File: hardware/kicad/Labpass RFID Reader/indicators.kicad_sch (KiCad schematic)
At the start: 8 parts

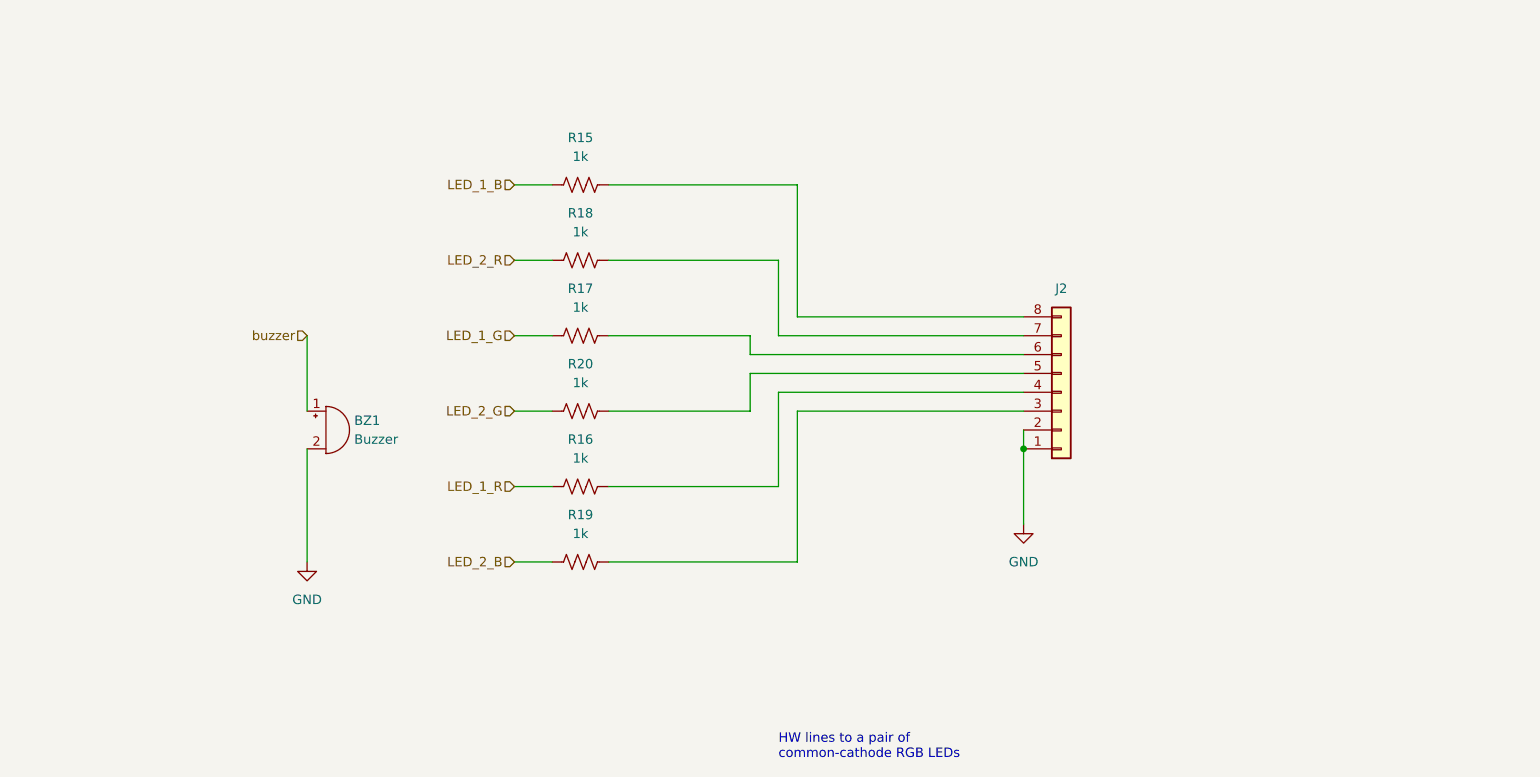
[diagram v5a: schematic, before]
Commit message: Add terminal block for gpio to ext relay
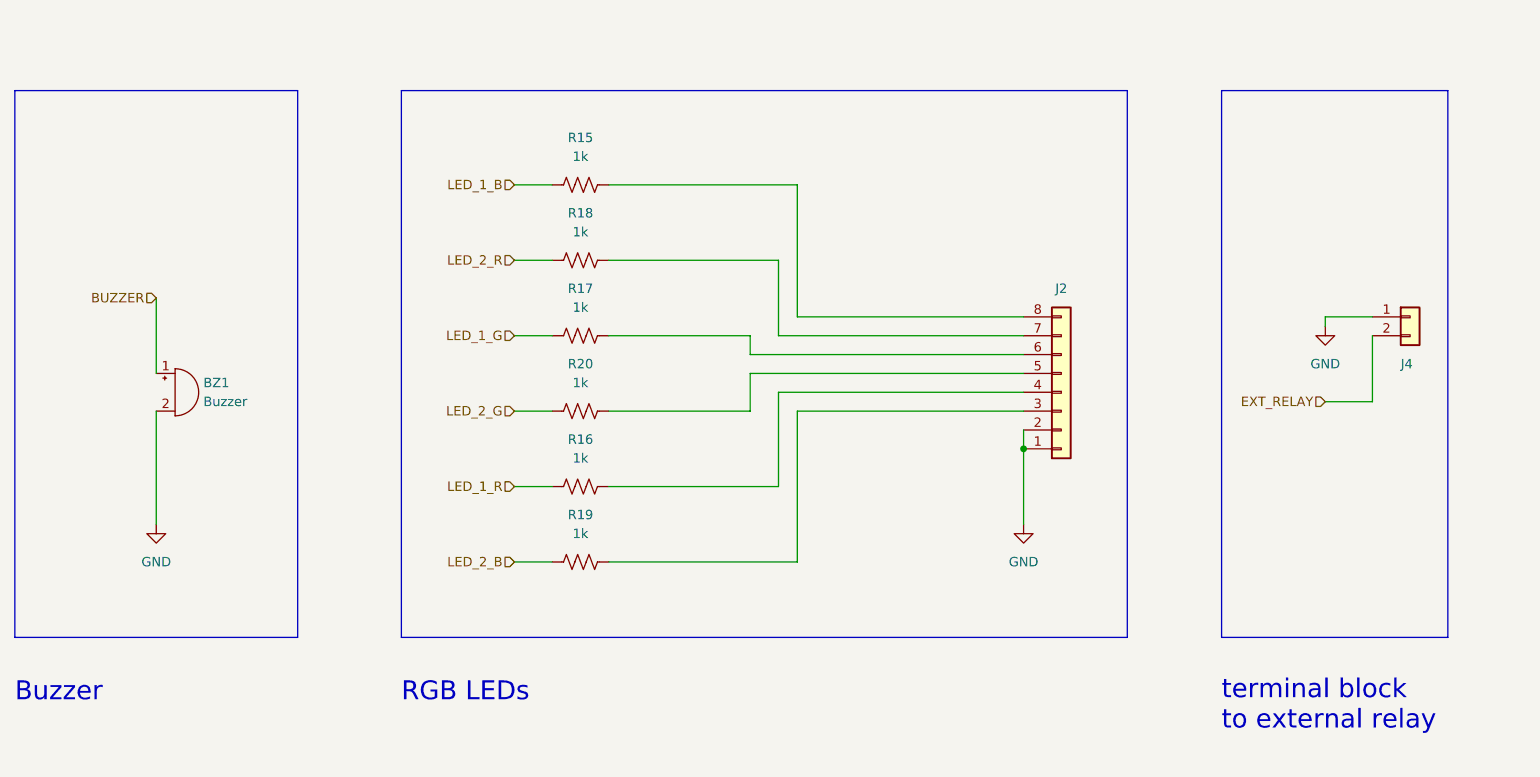
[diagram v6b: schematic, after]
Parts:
- added J4: (no value), symbol Connector_Generic:Conn_01x02
- J2: value (none) -> Conn_01x08; footprint (none) -> Connector_PinHeader_2.54mm:PinHeader_2x04_P2.54mm_Horizontal
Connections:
- net GND: now also J4.1 (Pin_1)
- net buzzer renamed BUZZER
- new net EXT_RELAY: J4.2 (Pin_2)
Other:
- note added: "Buzzer"
- note added: "RGB LEDs"
- note added: "terminal block to external relay"
- note removed: "HW lines to a pair of common-cathode RGB LEDs"
- moved on the sheet: BZ1
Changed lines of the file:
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@@
   (junction (at 167.64 97.79) (diameter 0) (color 0 0 0 0)
   )
+  (polyline (pts (xy 83.82 123.19) (xy 181.61 123.19))
+    (stroke (width 0) (type default) (color 0 0 0 0))
+  )
   (wire (pts (xy 130.81 92.71) (xy 130.81 87.63))
     (stroke (width 0) (type default) (color 0 0 0 0))
   )
-  (wire (pts (xy 71.12 82.55) (xy 71.12 92.71))
+  (wire (pts (xy 50.8 77.47) (xy 50.8 87.63))
+    (stroke (width 0) (type default) (color 0 0 0 0))
+  )
+  (polyline (pts (xy 31.75 49.53) (xy 31.75 123.19))
     (stroke (width 0) (type default) (color 0 0 0 0))
   )
@@
     (stroke (width 0) (type default) (color 0 0 0 0))
   )
+  (polyline (pts (xy 69.85 123.19) (xy 31.75 123.19))
+    (stroke (width 0) (type default) (color 0 0 0 0))
+  )
   (wire (pts (xy 99.06 82.55) (xy 104.14 82.55))
     (stroke (width 0) (type default) (color 0 0 0 0))
   )
+  (polyline (pts (xy 69.85 49.53) (xy 69.85 123.19))
+    (stroke (width 0) (type default) (color 0 0 0 0))
+  )
+  (wire (pts (xy 208.28 80.01) (xy 214.63 80.01))
+    (stroke (width 0) (type default) (color 0 0 0 0))
+  )
   (wire (pts (xy 99.06 102.87) (xy 104.14 102.87))
     (stroke (width 0) (type default) (color 0 0 0 0))
@@
     (stroke (width 0) (type default) (color 0 0 0 0))
   )
+  (polyline (pts (xy 194.31 49.53) (xy 224.79 49.53))
+    (stroke (width 0) (type default) (color 0 0 0 0))
+  )
   (wire (pts (xy 111.76 113.03) (xy 137.16 113.03))
     (stroke (width 0) (type default) (color 0 0 0 0))
   )
+  (wire (pts (xy 208.28 91.44) (xy 214.63 91.44))
+    (stroke (width 0) (type default) (color 0 0 0 0))
+  )
   (wire (pts (xy 111.76 102.87) (xy 134.62 102.87))
     (stroke (width 0) (type default) (color 0 0 0 0))
   )
+  (polyline (pts (xy 194.31 123.19) (xy 224.79 123.19))
+    (stroke (width 0) (type default) (color 0 0 0 0))
+  )
+  (polyline (pts (xy 224.79 123.19) (xy 224.79 49.53))
+    (stroke (width 0) (type default) (color 0 0 0 0))
+  )
   (wire (pts (xy 137.16 92.71) (xy 167.64 92.71))
     (stroke (width 0) (type default) (color 0 0 0 0))
   )
+  (wire (pts (xy 214.63 82.55) (xy 214.63 91.44))
+    (stroke (width 0) (type default) (color 0 0 0 0))
+  )
   (wire (pts (xy 99.06 72.39) (xy 104.14 72.39))
     (stroke (width 0) (type default) (color 0 0 0 0))
@@
     (stroke (width 0) (type default) (color 0 0 0 0))
   )
+  (polyline (pts (xy 83.82 49.53) (xy 83.82 123.19))
+    (stroke (width 0) (type default) (color 0 0 0 0))
+  )
   (wire (pts (xy 137.16 80.01) (xy 167.64 80.01))
     (stroke (width 0) (type default) (color 0 0 0 0))
@@
     (stroke (width 0) (type default) (color 0 0 0 0))
   )
+  (polyline (pts (xy 31.75 49.53) (xy 69.85 49.53))
+    (stroke (width 0) (type default) (color 0 0 0 0))
+  )
   (wire (pts (xy 130.81 82.55) (xy 130.81 85.09))
     (stroke (width 0) (type default) (color 0 0 0 0))
@@
     (stroke (width 0) (type default) (color 0 0 0 0))
   )
-  (wire (pts (xy 71.12 97.79) (xy 71.12 113.03))
+  (wire (pts (xy 50.8 92.71) (xy 50.8 107.95))
+    (stroke (width 0) (type default) (color 0 0 0 0))
+  )
+  (polyline (pts (xy 181.61 123.19) (xy 181.61 49.53))
     (stroke (width 0) (type default) (color 0 0 0 0))
   )
@@
     (stroke (width 0) (type default) (color 0 0 0 0))
   )
+  (polyline (pts (xy 83.82 49.53) (xy 181.61 49.53))
+    (stroke (width 0) (type default) (color 0 0 0 0))
+  )
+  (polyline (pts (xy 194.31 49.53) (xy 194.31 123.19))
+    (stroke (width 0) (type default) (color 0 0 0 0))
+  )
   (wire (pts (xy 99.06 113.03) (xy 104.14 113.03))
     (stroke (width 0) (type default) (color 0 0 0 0))
@@
     (stroke (width 0) (type default) (color 0 0 0 0))
   )
+  (wire (pts (xy 208.28 80.01) (xy 208.28 81.28))
+    (stroke (width 0) (type default) (color 0 0 0 0))
+  )
   (wire (pts (xy 137.16 62.23) (xy 137.16 80.01))
     (stroke (width 0) (type default) (color 0 0 0 0))
@@
     (stroke (width 0) (type default) (color 0 0 0 0))
   )
-  (text "HW lines to a pair of\ncommon-cathode RGB LEDs" (at 134.62 139.7 0)
-    (effects (font (size 1.27 1.27)) (justify left bottom))
+  (text "RGB LEDs\n" (at 83.82 132.08 0)
+    (effects (font (size 2.54 2.54)) (justify left bottom))
+  )
+  (text "terminal block\nto external relay" (at 194.31 135.89 0)
+    (effects (font (size 2.54 2.54)) (justify left bottom))
+  )
+  (text "Buzzer" (at 31.75 132.08 0)
+    (effects (font (size 2.54 2.54)) (justify left bottom))
+  )
+  (hierarchical_label "EXT_RELAY" (shape input) (at 208.28 91.44 180)
+    (effects (font (size 1.27 1.27)) (justify right))
   )
   (hierarchical_label "LED_2_R" (shape input) (at 99.06 72.39 180)
@@
     (effects (font (size 1.27 1.27)) (justify right))
   )
-  (hierarchical_label "buzzer" (shape input) (at 71.12 82.55 180)
+  (hierarchical_label "BUZZER" (shape input) (at 50.8 77.47 180)
     (effects (font (size 1.27 1.27)) (justify right))
   )
@@
   (hierarchical_label "LED_1_G" (shape input) (at 99.06 82.55 180)
     (effects (font (size 1.27 1.27)) (justify right))
+  )
+  (symbol (lib_id "power:GND") (at 208.28 81.28 0) (unit 1)
+    (in_bom yes) (on_board yes) (fields_autoplaced)
+    (property "Reference" "#PWR011" (id 0) (at 208.28 87.63 0)
+      (effects (font (size 1.27 1.27)) hide)
+    )
+    (property "Value" "GND" (id 1) (at 208.28 86.36 0))
+    (property "Footprint" "" (id 2) (at 208.28 81.28 0)
+      (effects (font (size 1.27 1.27)) hide)
+    )
+    (property "Datasheet" "" (id 3) (at 208.28 81.28 0)
+      (effects (font (size 1.27 1.27)) hide)
+    )
+    (pin "1")
   )
   (symbol (lib_id "Device:R_US") (at 107.95 102.87 90) (unit 1)
@@
     (pin "2")
   )
-  (symbol (lib_id "Device:Buzzer") (at 73.66 95.25 0) (unit 1)
-    (in_bom yes) (on_board yes) (fields_autoplaced)
-    (property "Reference" "BZ1" (id 0) (at 77.47 93.9799 0)
+  (symbol (lib_id "Device:Buzzer") (at 53.34 90.17 0) (unit 1)
+    (in_bom yes) (on_board yes) (fields_autoplaced)
+    (property "Reference" "BZ1" (id 0) (at 57.15 88.8999 0)
       (effects (font (size 1.27 1.27)) (justify left))
     )
-    (property "Value" "Buzzer" (id 1) (at 77.47 96.5199 0)
+    (property "Value" "Buzzer" (id 1) (at 57.15 91.4399 0)
       (effects (font (size 1.27 1.27)) (justify left))
     )
-    (property "Footprint" "Capstone Footprint Library:buzzer" (id 2) (at 73.025 92.71 90)
-      (effects (font (size 1.27 1.27)) hide)
-    )
-    (property "Datasheet" "~" (id 3) (at 73.025 92.71 90)
+    (property "Footprint" "Capstone Footprint Library:buzzer" (id 2) (at 52.705 87.63 90)
+      (effects (font (size 1.27 1.27)) hide)
+    )
+    (property "Datasheet" "~" (id 3) (at 52.705 87.63 90)
       (effects (font (size 1.27 1.27)) hide)
     )
@@
     (pin "2")
   )
-  (symbol (lib_id "power:GND") (at 71.12 113.03 0) (unit 1)
-    (in_bom yes) (on_board yes) (fields_autoplaced)
-    (property "Reference" "#PWR0101" (id 0) (at 71.12 119.38 0)
-      (effects (font (size 1.27 1.27)) hide)
-    )
-    (property "Value" "GND" (id 1) (at 71.12 118.11 0))
-    (property "Footprint" "" (id 2) (at 71.12 113.03 0)
-      (effects (font (size 1.27 1.27)) hide)
-    )
-    (property "Datasheet" "" (id 3) (at 71.12 113.03 0)
+  (symbol (lib_id "power:GND") (at 50.8 107.95 0) (unit 1)
+    (in_bom yes) (on_board yes) (fields_autoplaced)
+    (property "Reference" "#PWR0101" (id 0) (at 50.8 114.3 0)
+      (effects (font (size 1.27 1.27)) hide)
+    )
+    (property "Value" "GND" (id 1) (at 50.8 113.03 0))
+    (property "Footprint" "" (id 2) (at 50.8 107.95 0)
+      (effects (font (size 1.27 1.27)) hide)
+    )
+    (property "Datasheet" "" (id 3) (at 50.8 107.95 0)
       (effects (font (size 1.27 1.27)) hide)
     )
@@
     (in_bom yes) (on_board yes) (fields_autoplaced)
     (property "Reference" "J2" (id 0) (at 172.72 76.2 0))
-    (property "Value" "" (id 1) (at 179.07 88.9 90)
-      (effects (font (size 1.27 1.27)) hide)
-    )
-    (property "Footprint" "" (id 2) (at 172.72 90.17 0)
+    (property "Value" "Conn_01x08" (id 1) (at 179.07 88.9 90)
+      (effects (font (size 1.27 1.27)) hide)
+    )
+    (property "Footprint" "Connector_PinHeader_2.54mm:PinHeader_2x04_P2.54mm_Horizontal" (id 2) (at 172.72 90.17 0)
       (effects (font (size 1.27 1.27)) hide)
     )
@@
       (effects (font (size 1.27 1.27)) hide)
     )
+    (pin "1")
+    (pin "2")
+  )
+  (symbol (lib_id "Connector_Generic:Conn_01x02") (at 219.71 80.01 0) (unit 1)
+    (in_bom yes) (on_board yes)
+    (property "Reference" "J4" (id 0) (at 218.44 86.36 0)
+      (effects (font (size 1.27 1.27)) (justify left))
+    )
+    (property "Value" "" (id 1) (at 222.25 82.5499 0)
+      (effects (font (size 1.27 1.27)) (justify left) hide)
+    )
+    (property "Footprint" "" (id 2) (at 219.71 80.01 0)
+      (effects (font (size 1.27 1.27)) hide)
+    )
+    (property "Datasheet" "~" (id 3) (at 219.71 80.01 0)
+      (effects (font (size 1.27 1.27)) hide)
+    )

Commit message: bump rev to 1.0.0
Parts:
- J4: value (none) -> Conn_01x02; footprint (none) -> Capstone Footprint Library:Anytek NQ
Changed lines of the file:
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@@
       (effects (font (size 1.27 1.27)) (justify left))
     )
-    (property "Value" "" (id 1) (at 222.25 82.5499 0)
+    (property "Value" "Conn_01x02" (id 1) (at 222.25 82.5499 0)
       (effects (font (size 1.27 1.27)) (justify left) hide)
     )
-    (property "Footprint" "" (id 2) (at 219.71 80.01 0)
+    (property "Footprint" "Capstone Footprint Library:Anytek NQ" (id 2) (at 219.71 80.01 0)
       (effects (font (size 1.27 1.27)) hide)
     )
